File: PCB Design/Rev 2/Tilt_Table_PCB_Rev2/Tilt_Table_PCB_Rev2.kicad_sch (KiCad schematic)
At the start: 0 parts

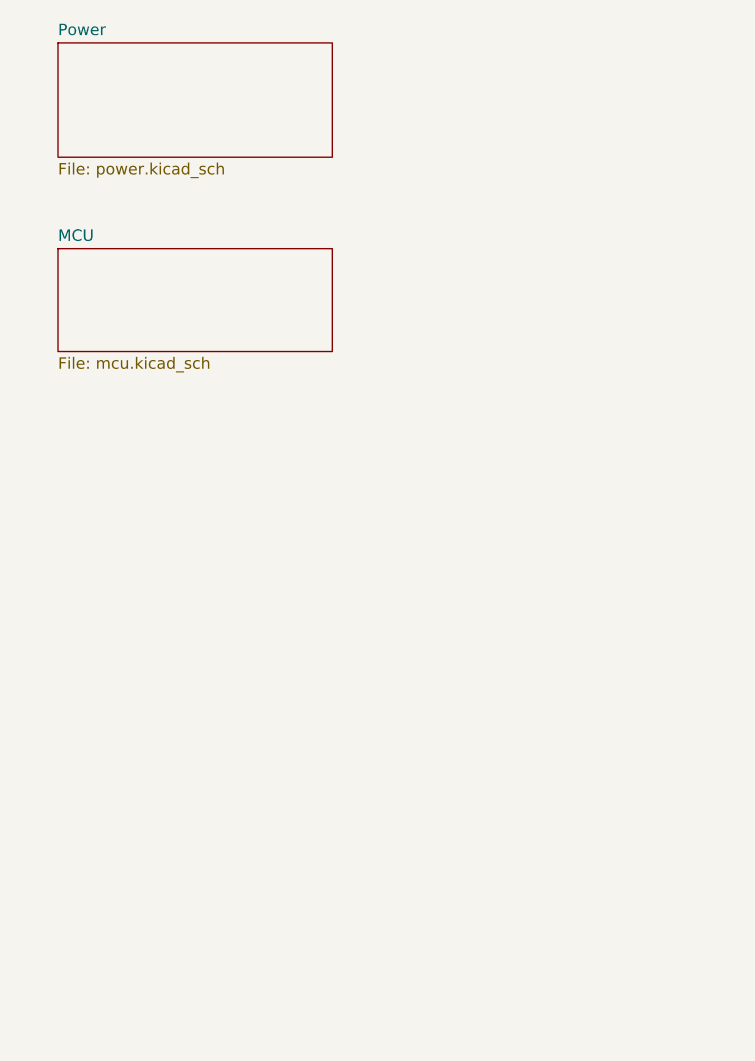
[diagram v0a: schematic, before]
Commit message: Rev 2 schematic updated
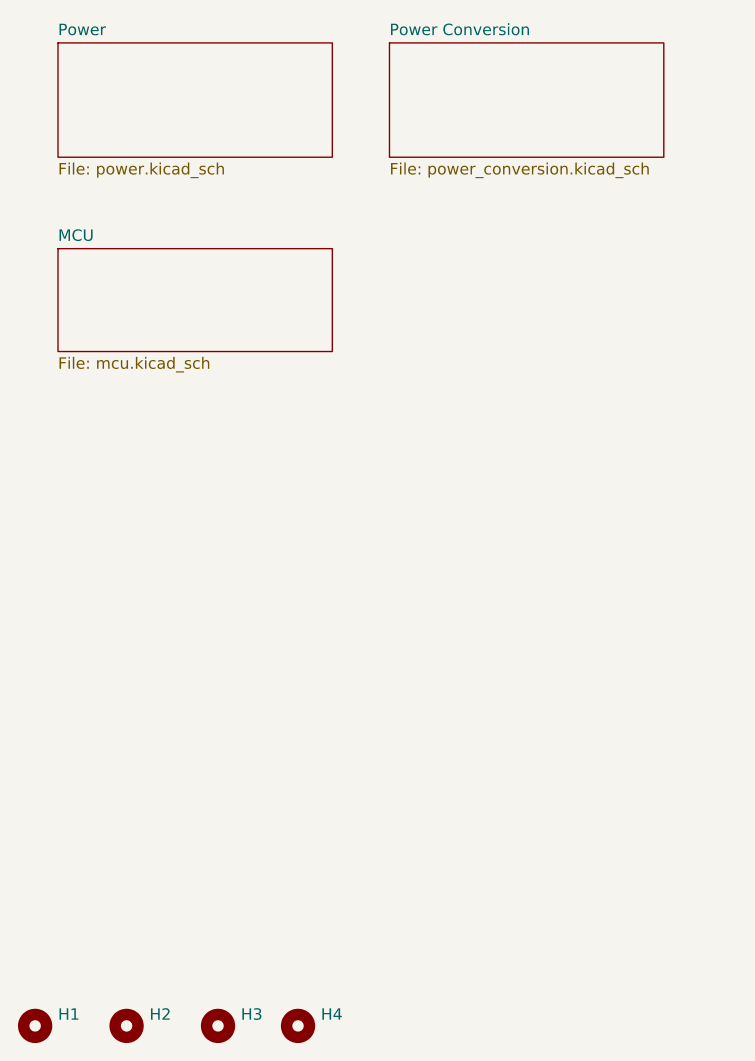
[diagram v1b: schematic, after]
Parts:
- added H1, H2, H3, H4: MountingHole, MountingHole:MountingHole_3.2mm_M3, symbol Mechanical:MountingHole
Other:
- added sheet Power Conversion (power_conversion.kicad_sch)

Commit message: PCB Rev 2 Update
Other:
- company: (none) -> Made by Jasper Tan
- title: (none) -> Tilt Plate Board
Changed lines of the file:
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@@
 	(generator_version "9.0")
 	(paper "A4")
+	(title_block
+		(title "Tilt Plate Board")
+		(date "2026-04-25")
+		(rev "2.0")
+		(company "Made by Jasper Tan")
+	)
 	(symbol
 		(lib_id "Mechanical:MountingHole")
